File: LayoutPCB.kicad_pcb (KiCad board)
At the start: 2 copper layers, 51.7 x 48.2 mm, 33 parts, among them J1 USB_B_Micro, J2 Conn_01x01_Female, J3 Conn_01x01_Female, J4 Conn_01x01_Female, J5 Conn_01x01_Female, J6 Conn_01x01_Female, J7 Conn_01x01_Female, U1 TP4056, U2 DW01, U3 FS8205A

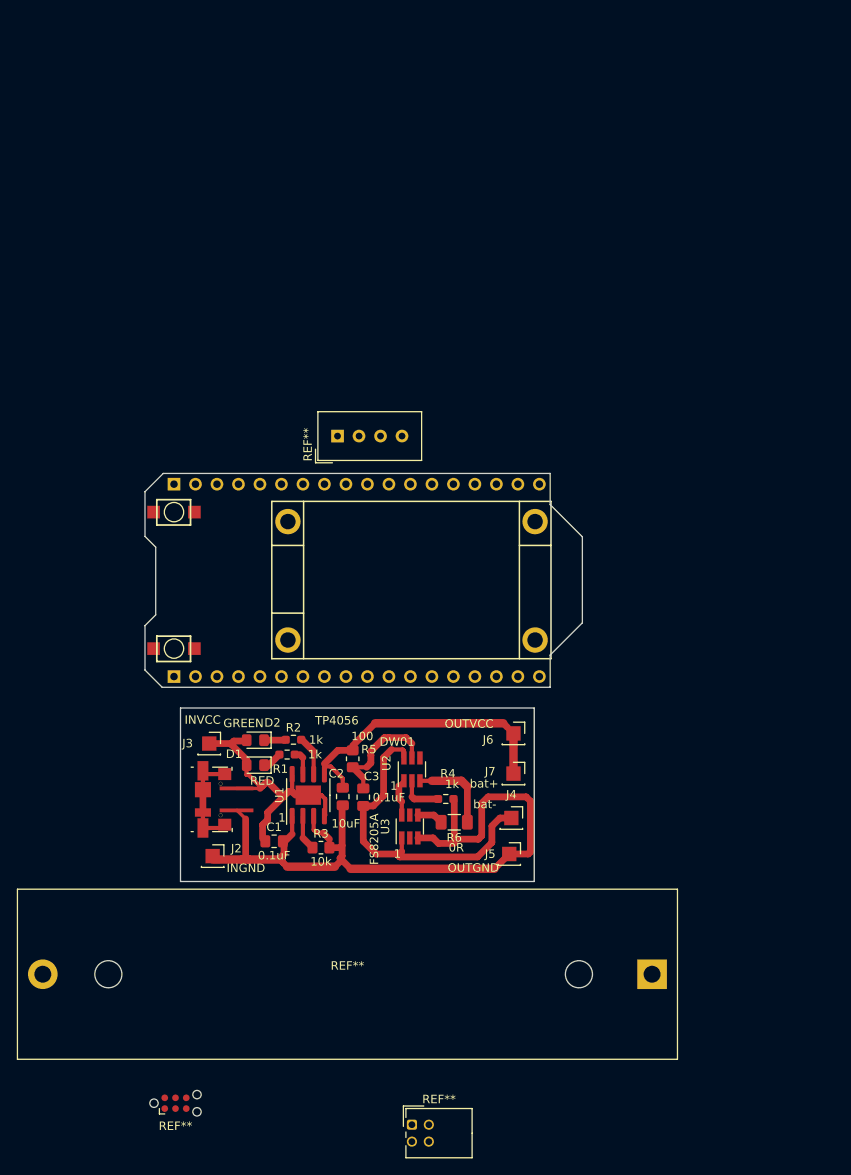
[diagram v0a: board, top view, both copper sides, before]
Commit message: Colocando mais componentes
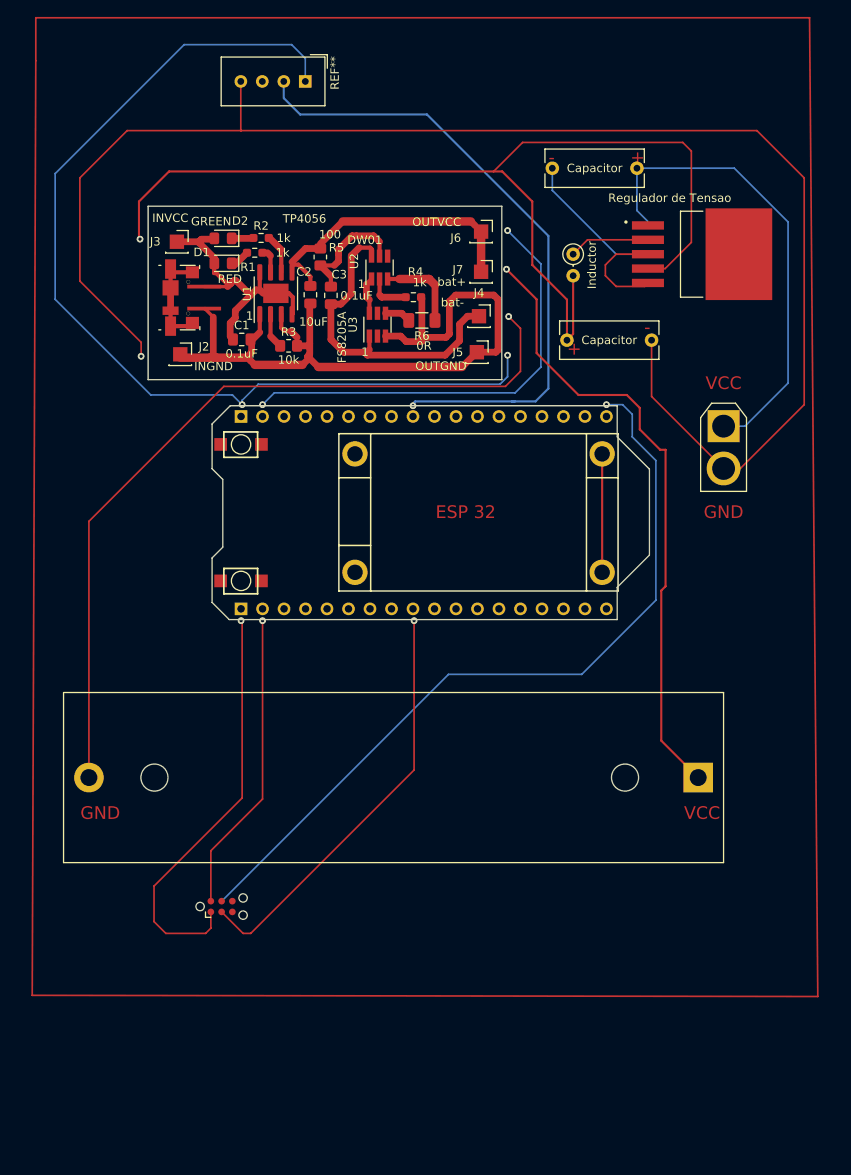
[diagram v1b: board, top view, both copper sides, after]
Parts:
- removed the REF** at (96.5, 162.6)
- added Capacitor : 220nF, Capacitor_THT:C_Rect_L11.5mm_W4.3mm_P10.00mm_MKT, F.Cu at (114.8, 69.8)
- added Capacitor : 680nF, Capacitor_THT:C_Rect_L11.5mm_W4.3mm_P10.00mm_MKT, F.Cu at (113.1, 49.5)
- added Inductor: 33uF, Inductor_THT:L_Axial_L5.3mm_D2.2mm_P2.54mm_Vertical_Vishay_IM-1, F.Cu at (115.6, 59.7)
- added REF**: Conector da Alimentação, Connector_AMASS:AMASS_XT30U-F_1x02_P5.0mm_Vertical, F.Cu at (133.3, 80.0)
- added Regulador de Tensao : LM2596S-5, LM2596S-5:TO170P1524X483-6N, F.Cu at (130.8, 59.7)
- REF**: value BatteryHolder_MPD_BH-18650-PC2 -> Bateria 18650
- REF**: value Tag-Connect_TC2030-IDC-NL_2x03_P1.27mm_Vertical -> Conector Display I2C
- moved C2 59.4 mm to (84.5, 64.5)
- moved C3 59.4 mm to (86.9, 64.6)
- moved D2 59.4 mm to (74.2, 57.8)
- moved J1 59.4 mm to (69.2, 64.8)
- moved U1 59.4 mm to (80.4, 64.3)
- moved D1 59.4 mm to (74.2, 60.8)
- moved J3 59.4 mm to (68.7, 58.2)
- moved J6 59.4 mm to (104.7, 57.0)
- moved J7 59.4 mm to (104.7, 61.8)
- moved R1 59.4 mm to (77.9, 59.5)
- moved R2 59.4 mm to (78.7, 57.8)
- moved R5 59.4 mm to (85.7, 60.0)
- moved U2 59.4 mm to (92.7, 61.3)
- moved C1 59.4 mm to (76.4, 69.8)
- moved J2 59.4 mm to (69.1, 71.5)
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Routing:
- net (no net): track 0.00 -> 1037.7 mm, vias 0 -> 14
- net GND: track 94.9 -> 108.9 mm
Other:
- board size 51.7 x 48.2 mm -> 59.2 x 48.9 mm
- board text added: "+"
- board text added: "-"
- board text added: "ESP 32"
- board text added: "GND"
- board text added: "VCC"

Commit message: Gerando os arquivos
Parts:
- added REF**: PinSocket_1x18_P2.54mm_Vertical, Connector_PinSocket_2.54mm:PinSocket_1x18_P2.54mm_Vertical, F.Cu at (76.3, 78.9)
- added REF**: PinSocket_1x18_P2.54mm_Vertical, Connector_PinSocket_2.54mm:PinSocket_1x18_P2.54mm_Vertical, F.Cu at (76.3, 101.6)
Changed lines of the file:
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@@
       (sketchpadsonfab false)
       (subtractmaskfromsilk false)
-      (outputformat 5)
-      (mirror true)
-      (drillshape 2)
+      (outputformat 1)
+      (mirror false)
+      (drillshape 0)
       (scaleselection 1)
       (outputdirectory "out/")
@@
   (net 17 "/G1")
   (net 18 "unconnected-(J1-Pad6)")
+  (footprint "Connector_PinSocket_2.54mm:PinSocket_1x18_P2.54mm_Vertical" (layer "F.Cu")
+    (at 76.327 78.867 90)
+    (descr "Through hole straight socket strip, 1x18, 2.54mm pitch, single row (from Kicad 4.0.7), script generated")
+    (tags "Through hole socket strip THT 1x18 2.54mm single row")
+    (attr through_hole)
+    (fp_text reference "REF**" (at 0 -2.77 90) (layer "F.SilkS")
+      (effects (font (size 1 1) (thickness 0.15)))
+    )
+    (fp_text value "PinSocket_1x18_P2.54mm_Vertical" (at 0 45.95 90) (layer "F.Fab")
+      (effects (font (size 1 1) (thickness 0.15)))
+    )
+    (fp_text user "${REFERENCE}" (at 0 21.59) (layer "F.Fab")
+      (effects (font (size 1 1) (thickness 0.15)))
+    )
+    (fp_line (start -1.33 1.27) (end 1.33 1.27) (layer "F.SilkS") (width 0.12))
+    (fp_line (start -1.33 1.27) (end -1.33 44.51) (layer "F.SilkS") (width 0.12))
+    (fp_line (start 0 -1.33) (end 1.33 -1.33) (layer "F.SilkS") (width 0.12))
+    (fp_line (start -1.33 44.51) (end 1.33 44.51) (layer "F.SilkS") (width 0.12))
+    (fp_line (start 1.33 -1.33) (end 1.33 0) (layer "F.SilkS") (width 0.12))
+    (fp_line (start 1.33 1.27) (end 1.33 44.51) (layer "F.SilkS") (width 0.12))
+    (fp_line (start 1.75 44.95) (end -1.8 44.95) (layer "F.CrtYd") (width 0.05))
+    (fp_line (start -1.8 44.95) (end -1.8 -1.8) (layer "F.CrtYd") (width 0.05))
+    (fp_line (start -1.8 -1.8) (end 1.75 -1.8) (layer "F.CrtYd") (width 0.05))
+    (fp_line (start 1.75 -1.8) (end 1.75 44.95) (layer "F.CrtYd") (width 0.05))
+    (fp_line (start 0.635 -1.27) (end 1.27 -0.635) (layer "F.Fab") (width 0.1))
+    (fp_line (start 1.27 -0.635) (end 1.27 44.45) (layer "F.Fab") (width 0.1))
+    (fp_line (start -1.27 44.45) (end -1.27 -1.27) (layer "F.Fab") (width 0.1))
+    (fp_line (start -1.27 -1.27) (end 0.635 -1.27) (layer "F.Fab") (width 0.1))
+    (fp_line (start 1.27 44.45) (end -1.27 44.45) (layer "F.Fab") (width 0.1))
+    (pad "1" thru_hole rect (at 0 0 90) (size 1.7 1.7) (drill 1) (layers *.Cu *.Mask))
+    (pad "2" thru_hole oval (at 0 2.54 90) (size 1.7 1.7) (drill 1) (layers *.Cu *.Mask))
+    (pad "3" thru_hole oval (at 0 5.08 90) (size 1.7 1.7) (drill 1) (layers *.Cu *.Mask))
+    (pad "4" thru_hole oval (at 0 7.62 90) (size 1.7 1.7) (drill 1) (layers *.Cu *.Mask))
+    (pad "5" thru_hole oval (at 0 10.16 90) (size 1.7 1.7) (drill 1) (layers *.Cu *.Mask))
+    (pad "6" thru_hole oval (at 0 12.7 90) (size 1.7 1.7) (drill 1) (layers *.Cu *.Mask))
+    (pad "7" thru_hole oval (at 0 15.24 90) (size 1.7 1.7) (drill 1) (layers *.Cu *.Mask))
+    (pad "8" thru_hole oval (at 0 17.78 90) (size 1.7 1.7) (drill 1) (layers *.Cu *.Mask))
+    (pad "9" thru_hole oval (at 0 20.32 90) (size 1.7 1.7) (drill 1) (layers *.Cu *.Mask))
+    (pad "10" thru_hole oval (at 0 22.86 90) (size 1.7 1.7) (drill 1) (layers *.Cu *.Mask))
+    (pad "11" thru_hole oval (at 0 25.4 90) (size 1.7 1.7) (drill 1) (layers *.Cu *.Mask))
+    (pad "12" thru_hole oval (at 0 27.94 90) (size 1.7 1.7) (drill 1) (layers *.Cu *.Mask))
+    (pad "13" thru_hole oval (at 0 30.48 90) (size 1.7 1.7) (drill 1) (layers *.Cu *.Mask))
+    (pad "14" thru_hole oval (at 0 33.02 90) (size 1.7 1.7) (drill 1) (layers *.Cu *.Mask))
+    (pad "15" thru_hole oval (at 0 35.56 90) (size 1.7 1.7) (drill 1) (layers *.Cu *.Mask))
+    (pad "16" thru_hole oval (at 0 38.1 90) (size 1.7 1.7) (drill 1) (layers *.Cu *.Mask))
+    (pad "17" thru_hole oval (at 0 40.64 90) (size 1.7 1.7) (drill 1) (layers *.Cu *.Mask))
+    (pad "18" thru_hole oval (at 0 43.18 90) (size 1.7 1.7) (drill 1) (layers *.Cu *.Mask))
+    (model "${KICAD6_3DMODEL_DIR}/Connector_PinSocket_2.54mm.3dshapes/PinSocket_1x18_P2.54mm_Vertical.wrl"
+      (offset (xyz 0 0 0))
+      (scale (xyz 1 1 1))
+      (rotate (xyz 0 0 0))
+    )
+  )
+  (footprint "Connector_PinSocket_2.54mm:PinSocket_1x18_P2.54mm_Vertical" (layer "F.Cu")
+    (at 76.327 101.6 90)
+    (descr "Through hole straight socket strip, 1x18, 2.54mm pitch, single row (from Kicad 4.0.7), script generated")
+    (tags "Through hole socket strip THT 1x18 2.54mm single row")
+    (attr through_hole)
+    (fp_text reference "REF**" (at 0 -2.77 90) (layer "F.SilkS")
+      (effects (font (size 1 1) (thickness 0.15)))
+    )
+    (fp_text value "PinSocket_1x18_P2.54mm_Vertical" (at 0 45.95 90) (layer "F.Fab")
+      (effects (font (size 1 1) (thickness 0.15)))
+    )
+    (fp_text user "${REFERENCE}" (at 0 21.59) (layer "F.Fab")
+      (effects (font (size 1 1) (thickness 0.15)))
+    )
+    (fp_line (start -1.33 44.51) (end 1.33 44.51) (layer "F.SilkS") (width 0.12))
+    (fp_line (start 1.33 -1.33) (end 1.33 0) (layer "F.SilkS") (width 0.12))
+    (fp_line (start -1.33 1.27) (end -1.33 44.51) (layer "F.SilkS") (width 0.12))
+    (fp_line (start 0 -1.33) (end 1.33 -1.33) (layer "F.SilkS") (width 0.12))
+    (fp_line (start 1.33 1.27) (end 1.33 44.51) (layer "F.SilkS") (width 0.12))
+    (fp_line (start -1.33 1.27) (end 1.33 1.27) (layer "F.SilkS") (width 0.12))
+    (fp_line (start -1.8 44.95) (end -1.8 -1.8) (layer "F.CrtYd") (width 0.05))
+    (fp_line (start 1.75 -1.8) (end 1.75 44.95) (layer "F.CrtYd") (width 0.05))
+    (fp_line (start 1.75 44.95) (end -1.8 44.95) (layer "F.CrtYd") (width 0.05))
+    (fp_line (start -1.8 -1.8) (end 1.75 -1.8) (layer "F.CrtYd") (width 0.05))
+    (fp_line (start -1.27 -1.27) (end 0.635 -1.27) (layer "F.Fab") (width 0.1))
+    (fp_line (start 0.635 -1.27) (end 1.27 -0.635) (layer "F.Fab") (width 0.1))
+    (fp_line (start 1.27 -0.635) (end 1.27 44.45) (layer "F.Fab") (width 0.1))
+    (fp_line (start 1.27 44.45) (end -1.27 44.45) (layer "F.Fab") (width 0.1))
+    (fp_line (start -1.27 44.45) (end -1.27 -1.27) (layer "F.Fab") (width 0.1))
+    (pad "1" thru_hole rect (at 0 0 90) (size 1.7 1.7) (drill 1) (layers *.Cu *.Mask))
+    (pad "2" thru_hole oval (at 0 2.54 90) (size 1.7 1.7) (drill 1) (layers *.Cu *.Mask))
+    (pad "3" thru_hole oval (at 0 5.08 90) (size 1.7 1.7) (drill 1) (layers *.Cu *.Mask))
+    (pad "4" thru_hole oval (at 0 7.62 90) (size 1.7 1.7) (drill 1) (layers *.Cu *.Mask))
+    (pad "5" thru_hole oval (at 0 10.16 90) (size 1.7 1.7) (drill 1) (layers *.Cu *.Mask))
+    (pad "6" thru_hole oval (at 0 12.7 90) (size 1.7 1.7) (drill 1) (layers *.Cu *.Mask))
+    (pad "7" thru_hole oval (at 0 15.24 90) (size 1.7 1.7) (drill 1) (layers *.Cu *.Mask))
+    (pad "8" thru_hole oval (at 0 17.78 90) (size 1.7 1.7) (drill 1) (layers *.Cu *.Mask))
+    (pad "9" thru_hole oval (at 0 20.32 90) (size 1.7 1.7) (drill 1) (layers *.Cu *.Mask))
+    (pad "10" thru_hole oval (at 0 22.86 90) (size 1.7 1.7) (drill 1) (layers *.Cu *.Mask))
+    (pad "11" thru_hole oval (at 0 25.4 90) (size 1.7 1.7) (drill 1) (layers *.Cu *.Mask))
+    (pad "12" thru_hole oval (at 0 27.94 90) (size 1.7 1.7) (drill 1) (layers *.Cu *.Mask))
+    (pad "13" thru_hole oval (at 0 30.48 90) (size 1.7 1.7) (drill 1) (layers *.Cu *.Mask))
+    (pad "14" thru_hole oval (at 0 33.02 90) (size 1.7 1.7) (drill 1) (layers *.Cu *.Mask))
+    (pad "15" thru_hole oval (at 0 35.56 90) (size 1.7 1.7) (drill 1) (layers *.Cu *.Mask))
+    (pad "16" thru_hole oval (at 0 38.1 90) (size 1.7 1.7) (drill 1) (layers *.Cu *.Mask))
+    (pad "17" thru_hole oval (at 0 40.64 90) (size 1.7 1.7) (drill 1) (layers *.Cu *.Mask))
+    (pad "18" thru_hole oval (at 0 43.18 90) (size 1.7 1.7) (drill 1) (layers *.Cu *.Mask))
+    (model "${KICAD6_3DMODEL_DIR}/Connector_PinSocket_2.54mm.3dshapes/PinSocket_1x18_P2.54mm_Vertical.wrl"
+      (offset (xyz 0 0 0))
+      (scale (xyz 1 1 1))
+      (rotate (xyz 0 0 0))
+    )
+  )
   (footprint "Connector_PinSocket_2.54mm:PinSocket_1x01_P2.54mm_Vertical" (layer "F.Cu")
     (at 104.1948 71.269)

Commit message: Colocando Nomes
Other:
- board text added: "Modulo da bateria"
- board text added: "Sensor de Temperatura/ Umidade"
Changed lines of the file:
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@@
+    (effects (font (size 1.5 1.5) (thickness 0.3)))
+  )
+  (gr_text "Modulo da bateria\n" (at 85.344 53.594) (layer "F.Cu")
+    (effects (font (size 1.5 1.5) (thickness 0.3)))
+  )
+  (gr_text "Sensor de Temperatura/ Umidade" (at 107.315 38.735) (layer "F.Cu")
     (effects (font (size 1.5 1.5) (thickness 0.3)))
   )

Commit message: Mais descrição
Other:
- board text added: "Placa de Sensor de Temperatua e Umidade ESP 32 com Lora e display OLED e Bateria Revisão 1.0 Autor Rafael Pascale"
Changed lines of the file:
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@@
+    (effects (font (size 1.5 1.5) (thickness 0.3)))
+  )
+  (gr_text "Placa de Sensor de Temperatua e Umidade \nESP 32 com Lora e display OLED e Bateria \nRevisão 1.0\nAutor Rafael Pascale" (at 117.221 140.462) (layer "F.Cu")
     (effects (font (size 1.5 1.5) (thickness 0.3)))
   )
@@
   (segment (start 76.327 102.997) (end 76.581 102.997) (width 0.2) (layer "F.Cu") (net 0))
   (segment (start 64.262 57.785) (end 64.389 57.912) (width 0.25) (layer "F.Cu") (net 0))
-  (segment (start 125.984 117.1747) (end 130.3483 121.539) (width 0.25) (layer "F.Cu") (net 0))
-  (segment (start 137.287 45.085) (end 76.327 45.085) (width 0.2) (layer "F.Cu") (net 0))
   (segment (start 111.252 71.374) (end 116.205 76.327) (width 0.25) (layer "F.Cu") (net 0))
   (segment (start 129.54 58.293) (end 129.54 47.498) (width 0.2) (layer "F.Cu") (net 0))
@@
   (segment (start 124.41 59.69) (end 120.65 59.69) (width 0.2) (layer "F.Cu") (net 0))
   (segment (start 126.492 98.933) (end 125.984 99.441) (width 0.25) (layer "F.Cu") (net 0))
-  (segment (start 142.875 50.673) (end 137.287 45.085) (width 0.2) (layer "F.Cu") (net 0))
   (segment (start 78.867 124.079) (end 72.7583 130.1877) (width 0.2) (layer "F.Cu") (net 0))
   (segment (start 128.524 46.482) (end 109.601 46.482) (width 0.2) (layer "F.Cu") (net 0))
+  (segment (start 107.696 61.468) (end 111.252 65.024) (width 0.25) (layer "F.Cu") (net 0))
   (segment (start 117.27 57.99) (end 115.57 59.69) (width 0.2) (layer "F.Cu") (net 0))
   (segment (start 72.7583 139.3317) (end 72.136 139.954) (width 0.2) (layer "F.Cu") (net 0))
   (segment (start 124.84 76.5) (end 133.35 85.01) (width 0.2) (layer "F.Cu") (net 0))
   (segment (start 133.35 85.01) (end 135.335 85.01) (width 0.2) (layer "F.Cu") (net 0))
-  (segment (start 142.875 77.47) (end 142.875 50.673) (width 0.2) (layer "F.Cu") (net 0))
-  (segment (start 126.492 82.804) (end 126.492 98.933) (width 0.25) (layer "F.Cu") (net 0))
-  (segment (start 121.92 76.327) (end 123.444 77.851) (width 0.25) (layer "F.Cu") (net 0))
   (segment (start 124 63.5) (end 124.41 63.09) (width 0.2) (layer "F.Cu") (net 0))
   (segment (start 76.2975 39.2725) (end 76.2975 45.0555) (width 0.2) (layer "F.Cu") (net 0))
   (segment (start 72.7583 137.414) (end 72.7583 139.3317) (width 0.2) (layer "F.Cu") (net 0))
-  (segment (start 107.696 61.468) (end 111.252 65.024) (width 0.25) (layer "F.Cu") (net 0))
   (segment (start 109.347 68.453) (end 109.347 73.533) (width 0.2) (layer "F.Cu") (net 0))
-  (segment (start 125.984 99.441) (end 125.984 117.1747) (width 0.25) (layer "F.Cu") (net 0))
-  (segment (start 111.252 65.024) (end 111.252 71.374) (width 0.25) (layer "F.Cu") (net 0))
   (segment (start 76.454 103.124) (end 76.327 102.997) (width 0.2) (layer "F.Cu") (net 0))
-  (segment (start 135.335 85.01) (end 142.875 77.47) (width 0.2) (layer "F.Cu") (net 0))
   (segment (start 76.5683 139.954) (end 74.0283 137.414) (width 0.2) (layer "F.Cu") (net 0))
   (segment (start 126.443 61.39) (end 129.54 58.293) (width 0.2) (layer "F.Cu") (net 0))
@@
   (segment (start 120.65 59.69) (end 119.38 60.96) (width 0.2) (layer "F.Cu") (net 0))
   (segment (start 109.347 73.533) (end 107.569 75.311) (width 0.2) (layer "F.Cu") (net 0))
-  (segment (start 125.857 82.804) (end 126.492 82.804) (width 0.25) (layer "F.Cu") (net 0))
   (segment (start 62.865 45.085) (end 57.277 50.673) (width 0.2) (layer "F.Cu") (net 0))
-  (segment (start 123.444 77.851) (end 123.444 80.391) (width 0.25) (layer "F.Cu") (net 0))
+  (segment (start 125.984 117.1747) (end 130.3483 121.539) (width 0.25) (layer "F.Cu") (net 0))
+  (segment (start 125.984 99.441) (end 125.984 117.1747) (width 0.25) (layer "F.Cu") (net 0))
   (segment (start 57.277 50.673) (end 57.277 62.865) (width 0.2) (layer "F.Cu") (net 0))
   (segment (start 67.818 49.911) (end 64.262 53.467) (width 0.25) (layer "F.Cu") (net 0))
+  (segment (start 123.444 80.391) (end 126.492 83.439) (width 0.25) (layer "F.Cu") (net 0))
+  (segment (start 121.92 76.327) (end 123.444 77.851) (width 0.25) (layer "F.Cu") (net 0))
   (segment (start 76.2975 45.0555) (end 76.327 45.085) (width 0.2) (layer "F.Cu") (net 0))
   (segment (start 115.57 69.12) (end 114.84 69.85) (width 0.25) (layer "F.Cu") (net 0))
   (segment (start 58.166 121.3567) (end 58.3483 121.539) (width 0.2) (layer "F.Cu") (net 0))
-  (segment (start 123.444 80.391) (end 125.857 82.804) (width 0.25) (layer "F.Cu") (net 0))
   (segment (start 110.744 53.467) (end 107.188 49.911) (width 0.25) (layer "F.Cu") (net 0))
   (segment (start 96.774 102.997) (end 96.774 120.65) (width 0.2) (layer "F.Cu") (net 0))
   (segment (start 107.95 67.056) (end 109.347 68.453) (width 0.2) (layer "F.Cu") (net 0))
+  (segment (start 142.875 77.47) (end 142.875 50.673) (width 0.2) (layer "F.Cu") (net 0))
   (segment (start 107.569 75.311) (end 74.295 75.311) (width 0.2) (layer "F.Cu") (net 0))
   (segment (start 109.601 46.482) (end 106.172 49.911) (width 0.2) (layer "F.Cu") (net 0))
@@
   (segment (start 72.136 139.954) (end 67.437 139.954) (width 0.2) (layer "F.Cu") (net 0))
   (segment (start 96.774 120.65) (end 77.47 139.954) (width 0.2) (layer "F.Cu") (net 0))
+  (segment (start 142.875 50.673) (end 137.287 45.085) (width 0.2) (layer "F.Cu") (net 0))
   (segment (start 57.277 62.865) (end 64.516 70.104) (width 0.2) (layer "F.Cu") (net 0))
   (segment (start 78.867 102.997) (end 78.867 124.079) (width 0.2) (layer "F.Cu") (net 0))
   (segment (start 58.3483 91.2577) (end 58.3483 121.539) (width 0.2) (layer "F.Cu") (net 0))
   (segment (start 106.172 49.911) (end 67.818 49.911) (width 0.25) (layer "F.Cu") (net 0))
+  (segment (start 137.287 45.085) (end 76.327 45.085) (width 0.2) (layer "F.Cu") (net 0))
   (segment (start 124.84 69.85) (end 124.84 76.5) (width 0.2) (layer "F.Cu") (net 0))
   (segment (start 107.188 49.911) (end 106.172 49.911) (width 0.25) (layer "F.Cu") (net 0))
@@
   (segment (start 124.41 61.39) (end 126.443 61.39) (width 0.2) (layer "F.Cu") (net 0))
   (segment (start 120.65 63.5) (end 124 63.5) (width 0.2) (layer "F.Cu") (net 0))
+  (segment (start 116.205 76.327) (end 121.92 76.327) (width 0.25) (layer "F.Cu") (net 0))
   (segment (start 115.57 62.23) (end 115.57 69.12) (width 0.25) (layer "F.Cu") (net 0))
   (segment (start 114.84 69.85) (end 114.84 65.056) (width 0.25) (layer "F.Cu") (net 0))
   (segment (start 76.327 45.085) (end 62.865 45.085) (width 0.2) (layer "F.Cu") (net 0))
-  (segment (start 116.205 76.327) (end 121.92 76.327) (width 0.25) (layer "F.Cu") (net 0))
+  (segment (start 135.335 85.01) (end 142.875 77.47) (width 0.2) (layer "F.Cu") (net 0))
   (segment (start 77.47 139.954) (end 76.5683 139.954) (width 0.2) (layer "F.Cu") (net 0))
+  (segment (start 126.492 83.439) (end 126.492 98.933) (width 0.25) (layer "F.Cu") (net 0))
   (segment (start 119.38 62.23) (end 120.65 63.5) (width 0.2) (layer "F.Cu") (net 0))
   (segment (start 66.04 138.557) (end 66.04 134.366) (width 0.2) (layer "F.Cu") (net 0))
@@
   (segment (start 119.38 60.96) (end 119.38 62.23) (width 0.2) (layer "F.Cu") (net 0))
   (segment (start 74.295 75.311) (end 58.3483 91.2577) (width 0.2) (layer "F.Cu") (net 0))
+  (segment (start 123.444 77.851) (end 123.444 80.391) (width 0.25) (layer "F.Cu") (net 0))
+  (segment (start 111.252 65.024) (end 111.252 71.374) (width 0.25) (layer "F.Cu") (net 0))
   (via (at 64.389 57.912) (size 0.8) (drill 0.4) (layers "F.Cu" "B.Cu") (free) (net 0))
   (via (at 107.696 61.468) (size 0.8) (drill 0.4) (layers "F.Cu" "B.Cu") (net 0))
